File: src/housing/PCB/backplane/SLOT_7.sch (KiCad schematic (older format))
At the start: 1 part, among them J8 10018784-10201TLF

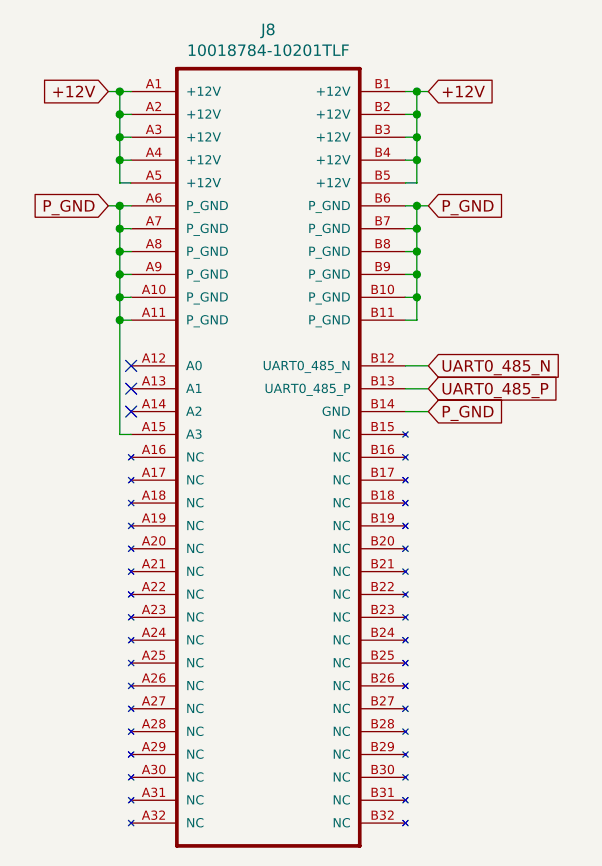
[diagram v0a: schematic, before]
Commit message: fixing backplane libraries path error
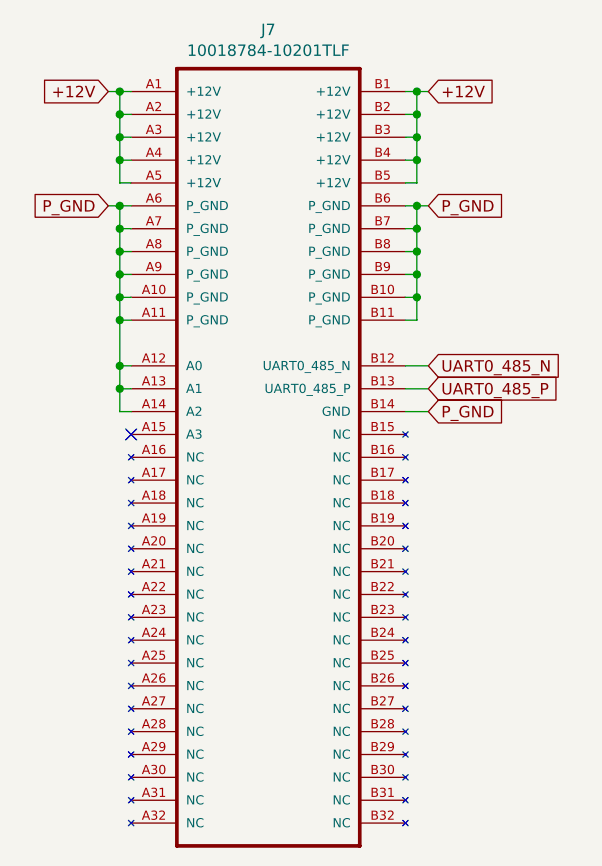
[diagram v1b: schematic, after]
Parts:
- removed J8: 10018784-10201TLF, kicad-lib:CONN_10018784-10201TLF, symbol 10018784-10201TLF:10018784-10201TLF
- added J7: 10018784-10201TLF, kicad-lib:CONN_10018784-10201TLF, symbol 10018784-10201TLF:10018784-10201TLF
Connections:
- net +12V: now also J7.A1 (+12V), J7.A2 (+12V), J7.A3 (+12V), J7.A4 (+12V), J7.A5 (+12V), J7.B1 (+12V), J7.B2 (+12V), J7.B3 (+12V), J7.B4 (+12V), J7.B5 (+12V)
- net P_GND: now also J7.A10 (P_GND), J7.A11 (P_GND), J7.A12 (A0), J7.A13 (A1), J7.A14 (A2), J7.A6 (P_GND), J7.A7 (P_GND), J7.A8 (P_GND), J7.A9 (P_GND), J7.B10 (P_GND), J7.B11 (P_GND), J7.B14 (GND), J7.B6 (P_GND), J7.B7 (P_GND), J7.B8 (P_GND), J7.B9 (P_GND)
- net UART0_485_N: now also J7.B12 (UART0_485_N)
- net UART0_485_P: now also J7.B13 (UART0_485_P)
- no-connect marks 3 -> 1
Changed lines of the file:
@@
 $Descr A4 11693 8268
 encoding utf-8
-Sheet 9 9
-Title ""
+Sheet 8 9
+Title "ACS backplane"
 Date ""
-Rev ""
-Comp ""
-Comment1 ""
+Rev "1"
+Comp "Halidelabs"
+Comment1 "contact@halidelabs.eu"
 Comment2 ""
 Comment3 ""
@@
 $Comp
 L 10018784-10201TLF:10018784-10201TLF J?
-U 1 1 5DF52F0A
+U 1 1 5DF52F0B
 P 5600 3950
-AR Path="/5DF19C0C/5DF52F0A" Ref="J?"  Part="1"
-AR Path="/5DF2A71E/5DF52F0A" Ref="J?"  Part="1"
-AR Path="/5DF2E10A/5DF52F0A" Ref="J?"  Part="1"
-AR Path="/5DF2E1F8/5DF52F0A" Ref="J?"  Part="1"
-AR Path="/5DF2E248/5DF52F0A" Ref="J?"  Part="1"
-AR Path="/5DF2E24C/5DF52F0A" Ref="J8"  Part="1"
-F 0 "J8" H 5600 5820 50  0000 C CNN
+AR Path="/5DF19C0C/5DF52F0B" Ref="J?"  Part="1"
+AR Path="/5DF2A71E/5DF52F0B" Ref="J?"  Part="1"
+AR Path="/5DF2E10A/5DF52F0B" Ref="J?"  Part="1"
+AR Path="/5DF2E1F6/5DF52F0B" Ref="J?"  Part="1"
+AR Path="/5DF2E246/5DF52F0B" Ref="J?"  Part="1"
+AR Path="/5DF2E24A/5DF52F0B" Ref="J7"  Part="1"
+F 0 "J7" H 5600 5820 50  0000 C CNN
 F 1 "10018784-10201TLF" H 5600 5729 50  0000 C CNN
 F 2 "kicad-lib:CONN_10018784-10201TLF" H 5650 4450 50  0001 L BNN
@@
 Wire Wire Line
 	6300 3750 6200 3750
+Wire Wire Line
+	4950 3350 4950 3550
+Wire Wire Line
+	4950 3550 5000 3550
 Connection ~ 4950 3350
 Wire Wire Line
-	4950 3850 5000 3850
+	4950 3550 4950 3650
 Wire Wire Line
-	4950 3350 4950 3850
-NoConn ~ 5000 3550
-NoConn ~ 5000 3650
-NoConn ~ 5000 3750
+	4950 3650 5000 3650
+Connection ~ 4950 3550
+Wire Wire Line
+	4950 3650 4950 3750
+Wire Wire Line
+	4950 3750 5000 3750
+Connection ~ 4950 3650
+NoConn ~ 5000 3850
 $EndSCHEMATC
